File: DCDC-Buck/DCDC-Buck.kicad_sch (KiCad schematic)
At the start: 0 parts

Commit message: Adding more to the project.
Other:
- added sheet COMPENSATOR (COMPENSATOR.kicad_sch)
- added sheet CONTROLLER (CONTROLLER.kicad_sch)
- added sheet INPUT (INPUT.kicad_sch)
- added sheet OUTPUT (OUTPUT.kicad_sch)
- added sheet PLANT (PLANT.kicad_sch)
- company: (none) -> Author: Ygor K.
- title: (none) -> MAIN

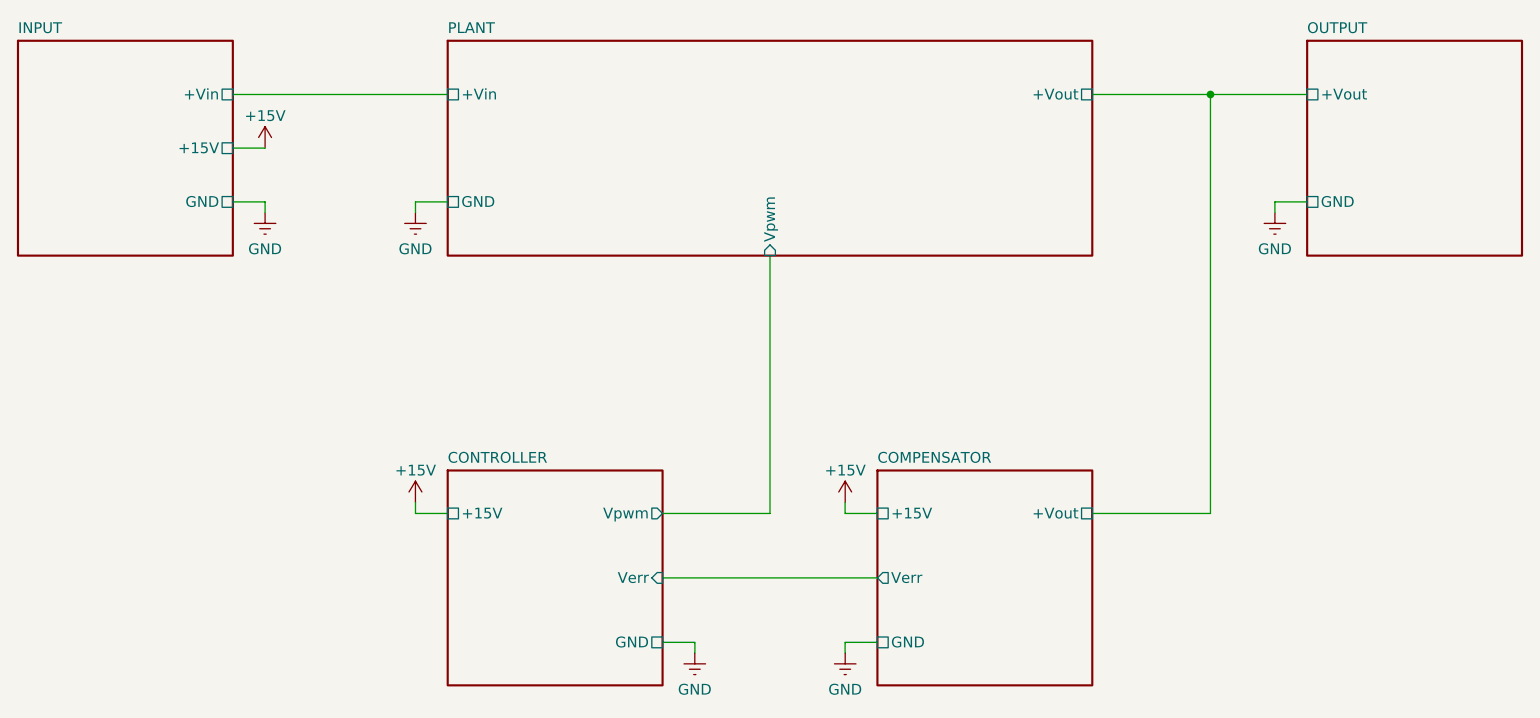
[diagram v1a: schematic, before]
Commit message: Finishing PCB design with 2 layers.
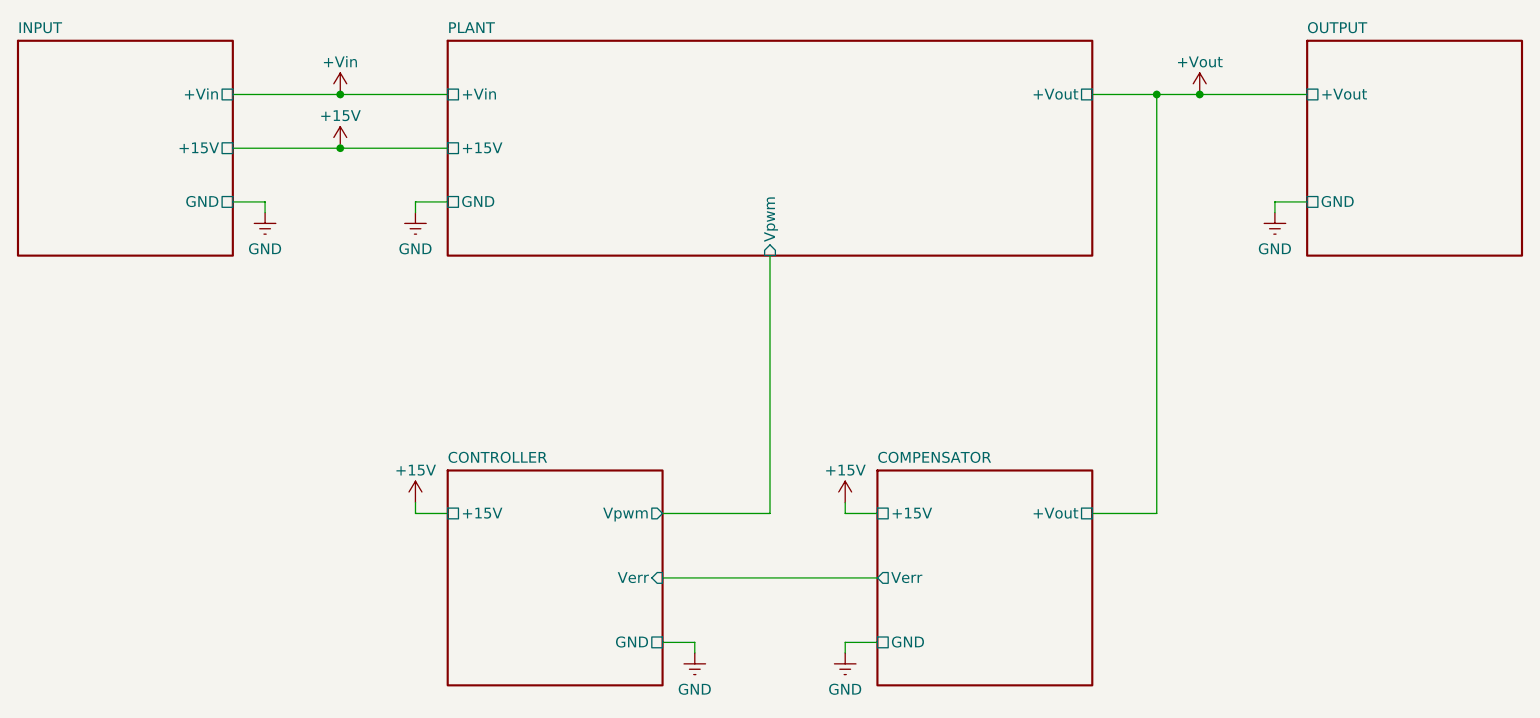
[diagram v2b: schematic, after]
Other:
- sheet PLANT ports: added +15V; removed none
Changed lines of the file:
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@@
 	(title_block
 		(title "MAIN")
+		(date "2026-09-27")
 		(rev "A")
 		(company "Author: Ygor K.")
 	)
 	(junction
-		(at 217.17 57.15)
+		(at 114.3 63.5)
 		(diameter 0)
 		(color 0 0 0 0)
 	)
+	(junction
+		(at 215.9 57.15)
+		(diameter 0)
+		(color 0 0 0 0)
+	)
+	(junction
+		(at 114.3 57.15)
+		(diameter 0)
+		(color 0 0 0 0)
+	)
+	(junction
+		(at 210.82 57.15)
+		(diameter 0)
+		(color 0 0 0 0)
+	)
 	(wire
 		(pts
@@
 	(wire
 		(pts
-			(xy 203.2 106.68) (xy 217.17 106.68)
-		)
-		(stroke
-			(width 0)
-			(type default)
-		)
-	)
-	(wire
-		(pts
-			(xy 217.17 106.68) (xy 217.17 57.15)
+			(xy 203.2 106.68) (xy 210.82 106.68)
+		)
+		(stroke
+			(width 0)
+			(type default)
+		)
+	)
+	(wire
+		(pts
+			(xy 210.82 106.68) (xy 210.82 57.15)
 		)
 		(stroke
@@
 	(wire
 		(pts
-			(xy 101.6 63.5) (xy 105.41 63.5)
+			(xy 101.6 63.5) (xy 127 63.5)
 		)
 		(stroke
@@
 	(wire
 		(pts
+			(xy 114.3 57.15) (xy 127 57.15)
+		)
+		(stroke
+			(width 0)
+			(type default)
+		)
+	)
+	(wire
+		(pts
 			(xy 123.19 105.41) (xy 123.19 106.68)
 		)
@@
 	(wire
 		(pts
-			(xy 101.6 57.15) (xy 127 57.15)
-		)
-		(stroke
-			(width 0)
-			(type default)
-		)
-	)
-	(wire
-		(pts
-			(xy 203.2 57.15) (xy 217.17 57.15)
+			(xy 101.6 57.15) (xy 114.3 57.15)
+		)
+		(stroke
+			(width 0)
+			(type default)
+		)
+	)
+	(wire
+		(pts
+			(xy 203.2 57.15) (xy 228.6 57.15)
 		)
 		(stroke
@@
 		(pts
 			(xy 152.4 114.3) (xy 177.8 114.3)
-		)
-		(stroke
-			(width 0)
-			(type default)
-		)
-	)
-	(wire
-		(pts
-			(xy 217.17 57.15) (xy 228.6 57.15)
 		)
 		(stroke
@@
 		(in_pos_files yes)
 		(dnp no)
-		(property "Reference" "#PWR04"
+		(property "Reference" "#PWR09"
 			(at 156.21 129.54 0)
 			(hide yes)
@@
 			(project "DCDC-Buck"
 				(path "/959e3d1c-01d0-4c7d-bf19-165b598aa596"
-					(reference "#PWR04")
+					(reference "#PWR09")
 					(unit 1)
 				)
@@
 		(in_pos_files yes)
 		(dnp no)
-		(property "Reference" "#PWR01"
+		(property "Reference" "#PWR05"
 			(at 123.19 77.47 0)
 			(hide yes)
@@
 			(project "DCDC-Buck"
 				(path "/959e3d1c-01d0-4c7d-bf19-165b598aa596"
-					(reference "#PWR01")
+					(reference "#PWR05")
+					(unit 1)
+				)
+			)
+		)
+	)
+	(symbol
+		(lib_id "power:VCC")
+		(at 215.9 57.15 0)
+		(unit 1)
+		(body_style 1)
+		(exclude_from_sim no)
+		(in_bom yes)
+		(on_board yes)
+		(in_pos_files yes)
+		(dnp no)
+		(property "Reference" "#PWR02"
+			(at 215.9 60.96 0)
+			(hide yes)
+			(show_name no)
+			(do_not_autoplace no)
+			(effects
+				(font
+					(size 1.27 1.27)
+				)
+			)
+		)
+		(property "Value" "+Vout"
+			(at 215.9 53.34 0)
+			(show_name no)
+			(do_not_autoplace no)
+			(effects
+				(font
+					(size 1.27 1.27)
+				)
+			)
+		)
+		(property "Footprint" ""
+			(at 215.9 57.15 0)
+			(hide yes)
+			(show_name no)
+			(do_not_autoplace no)
+			(effects
+				(font
+					(size 1.27 1.27)
+				)
+			)
+		)
+		(property "Datasheet" ""
+			(at 215.9 57.15 0)
+			(hide yes)
+			(show_name no)
+			(do_not_autoplace no)
+			(effects
+				(font
+					(size 1.27 1.27)
+				)
+			)
+		)
+		(property "Description" "Power symbol creates a global label with name \"VCC\""
+			(at 215.9 57.15 0)
+			(hide yes)
+			(show_name no)
+			(do_not_autoplace no)
+			(effects
+				(font
+					(size 1.27 1.27)
+				)
+			)
+		)
+		(pin "1"
+		)
+		(instances
+			(project "DCDC-Buck"
+				(path "/959e3d1c-01d0-4c7d-bf19-165b598aa596"
+					(reference "#PWR02")
 					(unit 1)
 				)
@@
 		(in_pos_files yes)
 		(dnp no)
-		(property "Reference" "#PWR02"
+		(property "Reference" "#PWR06"
 			(at 224.79 77.47 0)
 			(hide yes)
@@
 			(project "DCDC-Buck"
 				(path "/959e3d1c-01d0-4c7d-bf19-165b598aa596"
-					(reference "#PWR02")
+					(reference "#PWR06")
+					(unit 1)
+				)
+			)
+		)
+	)
+	(symbol
+		(lib_id "power:VCC")
+		(at 114.3 57.15 0)
+		(unit 1)
+		(body_style 1)
+		(exclude_from_sim no)
+		(in_bom yes)
+		(on_board yes)
+		(in_pos_files yes)
+		(dnp no)
+		(property "Reference" "#PWR01"
+			(at 114.3 60.96 0)
+			(hide yes)
+			(show_name no)
+			(do_not_autoplace no)
+			(effects
+				(font
+					(size 1.27 1.27)
+				)
+			)
+		)
+		(property "Value" "+Vin"
+			(at 114.3 53.34 0)
+			(show_name no)
+			(do_not_autoplace no)
+			(effects
+				(font
+					(size 1.27 1.27)
+				)
+			)
+		)
+		(property "Footprint" ""
+			(at 114.3 57.15 0)
+			(hide yes)
+			(show_name no)
+			(do_not_autoplace no)
+			(effects
+				(font
+					(size 1.27 1.27)
+				)
+			)
+		)
+		(property "Datasheet" ""
+			(at 114.3 57.15 0)
+			(hide yes)
+			(show_name no)
+			(do_not_autoplace no)
+			(effects
+				(font
+					(size 1.27 1.27)
+				)
+			)
+		)
+		(property "Description" "Power symbol creates a global label with name \"VCC\""
+			(at 114.3 57.15 0)
+			(hide yes)
+			(show_name no)
+			(do_not_autoplace no)
+			(effects
+				(font
+					(size 1.27 1.27)
+				)
+			)
+		)
+		(pin "1"
+		)
+		(instances
+			(project "DCDC-Buck"
+				(path "/959e3d1c-01d0-4c7d-bf19-165b598aa596"
+					(reference "#PWR01")
 					(unit 1)
 				)
@@
 		(in_pos_files yes)
 		(dnp no)
-		(property "Reference" "#PWR010"
+		(property "Reference" "#PWR08"
 			(at 173.99 109.22 0)
 			(hide yes)
@@
 			(project "DCDC-Buck"
 				(path "/959e3d1c-01d0-4c7d-bf19-165b598aa596"
-					(reference "#PWR010")
+					(reference "#PWR08")
 					(unit 1)
 				)
@@
 		(in_pos_files yes)
 		(dnp no)
-		(property "Reference" "#PWR03"
+		(property "Reference" "#PWR010"
 			(at 173.99 129.54 0)
 			(hide yes)
@@
 			(project "DCDC-Buck"
 				(path "/959e3d1c-01d0-4c7d-bf19-165b598aa596"
-					(reference "#PWR03")
+					(reference "#PWR010")
 					(unit 1)
 				)
@@
 		(in_pos_files yes)
 		(dnp no)
-		(property "Reference" "#PWR05"
+		(property "Reference" "#PWR04"
 			(at 105.41 77.47 0)
 			(hide yes)
@@
 			(project "DCDC-Buck"
 				(path "/959e3d1c-01d0-4c7d-bf19-165b598aa596"
-					(reference "#PWR05")
+					(reference "#PWR04")
 					(unit 1)
 				)
@@
 		(in_pos_files yes)
 		(dnp no)
-		(property "Reference" "#PWR09"
+		(property "Reference" "#PWR07"
 			(at 123.19 109.22 0)
 			(hide yes)
@@
 			(project "DCDC-Buck"
 				(path "/959e3d1c-01d0-4c7d-bf19-165b598aa596"
-					(reference "#PWR09")
+					(reference "#PWR07")
 					(unit 1)
 				)
@@
 	(symbol
 		(lib_id "power:VCC")
-		(at 105.41 63.5 0)
+		(at 114.3 63.5 0)
 		(unit 1)
 		(body_style 1)
@@
 		(in_pos_files yes)
 		(dnp no)
-		(property "Reference" "#PWR08"
-			(at 105.41 67.31 0)
+		(property "Reference" "#PWR03"
+			(at 114.3 67.31 0)
 			(hide yes)
 			(show_name no)
@@
 		)
 		(property "Value" "+15V"
-			(at 105.41 59.69 0)
+			(at 114.3 59.69 0)
 			(show_name no)
 			(do_not_autoplace no)
@@
 		)
 		(property "Footprint" ""
-			(at 105.41 63.5 0)
+			(at 114.3 63.5 0)
 			(hide yes)
 			(show_name no)
@@
 		)
 		(property "Datasheet" ""
-			(at 105.41 63.5 0)
+			(at 114.3 63.5 0)
 			(hide yes)
 			(show_name no)
@@
 		)
 		(property "Description" "Power symbol creates a global label with name \"VCC\""
-			(at 105.41 63.5 0)
+			(at 114.3 63.5 0)
 			(hide yes)
 			(show_name no)
@@
 			(project "DCDC-Buck"
 				(path "/959e3d1c-01d0-4c7d-bf19-165b598aa596"
-					(reference "#PWR08")
+					(reference "#PWR03")
 					(unit 1)
 				)
@@
 			(effects
 				(font
+					(size 1.27 1.27)
+				)
+				(justify left)
+			)
+		)
+		(pin "+15V" passive
+			(at 127 63.5 180)
+			(effects
+				(font
